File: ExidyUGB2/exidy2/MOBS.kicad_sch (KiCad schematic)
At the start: 22 parts, among them U10F_ 74LS04, U11E 74LS193, U11F_ 74LS04, U12E 74LS193, U13E 74LS193, U13F 74LS193, U14F 74LS193, U15F 74LS193, U16E 74LS193, U16F 74LS193, U16H_ 74LS139, U3F_ 74LS04, U5E 74LS08, U6F_ 74LS32

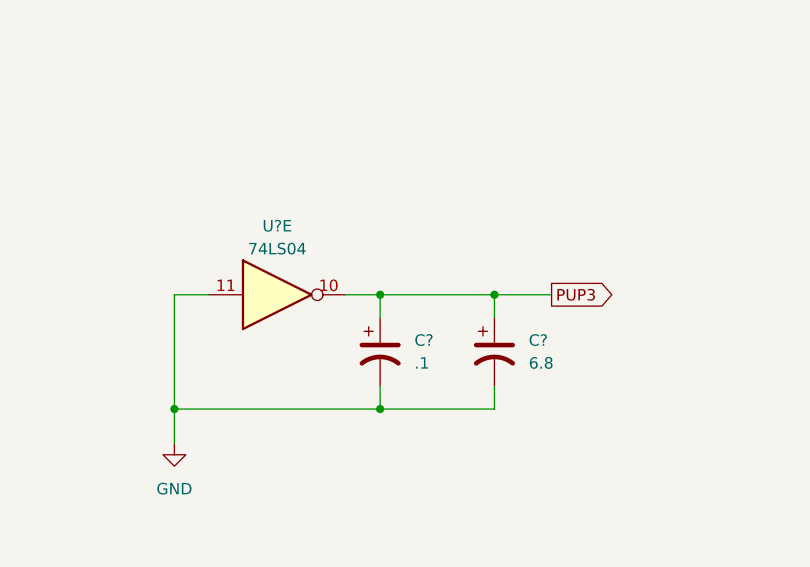
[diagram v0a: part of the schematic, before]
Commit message: Updates to KiCAD8
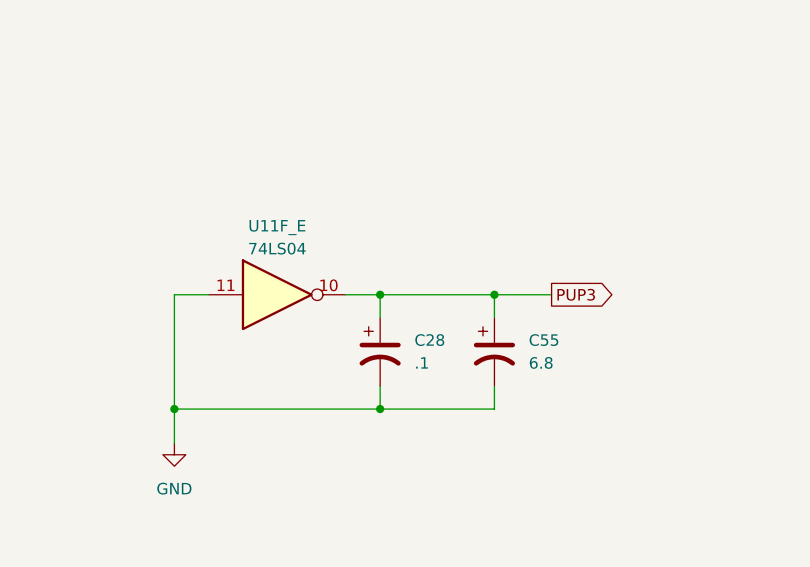
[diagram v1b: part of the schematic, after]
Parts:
- gave numbers to parts that had none: 3
